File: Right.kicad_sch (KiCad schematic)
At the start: 27 parts, among them J2 Conn_01x02, J4 USB_B_Micro, U1 NCP1117-3.3_SOT223, U2 W25Q128JVS, U3 RP2040, Y1 ECS-120-8-33-JGN-TR3

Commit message: Schematic mostly finished
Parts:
- removed J4: USB_B_Micro, symbol arisu-split:USB_B_Micro
- removed Y1: ECS-120-8-33-JGN-TR3, Crystal:Crystal_SMD_EuroQuartz_MT-4Pin_3.2x2.5mm, symbol Device:Crystal
- added J4: 10103594-0001LF, arisu-split:USB_Micro-B_Amphenol_10103594-0001LF_Horizontal, symbol arisu-split:10103594-0001LF
- added Y1: ECS-120-8-33-JGN-TR3, Crystal:Crystal_SMD_EuroQuartz_MT-4Pin_3.2x2.5mm, symbol Device:Crystal_GND24
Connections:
- net GND_R: now also J4.5 (GND), J4.6 (Shield), Y1.2, Y1.4
- net USB_D+: now also J4.3 (D+)
- net USB_D-: now also J4.2 (D-)
- net XIN: now also Y1.1
- net at C2.1, R3.2: now also Y1.3
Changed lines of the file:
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@@
     (effects (font (size 2.54 2.54)) (justify left bottom))
   )
-  (text "12MHz\n" (at 49.53 161.29 0)
+  (text "12MHz\n" (at 50.8 157.48 0)
     (effects (font (size 1.27 1.27)) (justify left bottom))
   )
@@
     (pin "2")
   )
+  (symbol (lib_id "Device:Crystal_GND24") (at 45.72 158.75 270) (unit 1)
+    (in_bom yes) (on_board yes)
+    (property "Reference" "Y1" (id 0) (at 44.45 148.59 90)
+      (effects (font (size 1.27 1.27)) (justify left))
+    )
+    (property "Value" "ECS-120-8-33-JGN-TR3" (id 1) (at 34.29 151.13 90)
+      (effects (font (size 1.27 1.27)) (justify left))
+    )
+    (property "Footprint" "Crystal:Crystal_SMD_EuroQuartz_MT-4Pin_3.2x2.5mm" (id 2) (at 45.72 158.75 0)
+      (effects (font (size 1.27 1.27)) hide)
+    )
+    (property "Datasheet" "~" (id 3) (at 45.72 158.75 0)
+      (effects (font (size 1.27 1.27)) hide)
+    )
+    (pin "1")
+    (pin "2")
+    (pin "3")
+    (pin "4")
+  )
   (symbol (lib_id "Device:C") (at 251.46 33.02 0) (unit 1)
     (in_bom yes) (on_board yes)
@@
     (pin "1")
   )
-  (symbol (lib_id "Device:Crystal") (at 45.72 158.75 270) (unit 1)
-    (in_bom yes) (on_board yes)
-    (property "Reference" "Y1" (id 0) (at 49.0474 157.5816 90)
-      (effects (font (size 1.27 1.27)) (justify left))
-    )
-    (property "Value" "ECS-120-8-33-JGN-TR3" (id 1) (at 34.29 151.13 90)
-      (effects (font (size 1.27 1.27)) (justify left))
-    )
-    (property "Footprint" "Crystal:Crystal_SMD_EuroQuartz_MT-4Pin_3.2x2.5mm" (id 2) (at 45.72 158.75 0)
-      (effects (font (size 1.27 1.27)) hide)
-    )
-    (property "Datasheet" "~" (id 3) (at 45.72 158.75 0)
-      (effects (font (size 1.27 1.27)) hide)
-    )
-    (pin "1")
-    (pin "2")
-  )
   (symbol (lib_id "arisu-split:GND_R") (at 102.87 38.1 0) (unit 1)
     (in_bom yes) (on_board yes) (fields_autoplaced)
@@
     (pin "1")
   )
-  (symbol (lib_id "Device:C") (at 194.31 48.26 0) (unit 1)
-    (in_bom yes) (on_board yes)
-    (property "Reference" "C10" (id 0) (at 197.231 47.0916 0)
-      (effects (font (size 1.27 1.27)) (justify left))
-    )
-    (property "Value" "1u" (id 1) (at 197.231 49.403 0)
-      (effects (font (size 1.27 1.27)) (justify left))
-    )
-    (property "Footprint" "Capacitor_SMD:C_0402_1005Metric" (id 2) (at 195.2752 52.07 0)
-      (effects (font (size 1.27 1.27)) hide)
-    )
-    (property "Datasheet" "~" (id 3) (at 194.31 48.26 0)
-      (effects (font (size 1.27 1.27)) hide)
-    )
-    (pin "1")
-    (pin "2")
-  )
-  (symbol (lib_id "Device:C") (at 30.48 163.83 270) (unit 1)
-    (in_bom yes) (on_board yes)
-    (property "Reference" "C2" (id 0) (at 31.6484 166.751 0)
-      (effects (font (size 1.27 1.27)) (justify left))
-    )
-    (property "Value" "30p" (id 1) (at 29.337 166.751 0)
-      (effects (font (size 1.27 1.27)) (justify left))
-    )
-    (property "Footprint" "Capacitor_SMD:C_0402_1005Metric" (id 2) (at 26.67 164.7952 0)
-      (effects (font (size 1.27 1.27)) hide)
-    )
-    (property "Datasheet" "~" (id 3) (at 30.48 163.83 0)
-      (effects (font (size 1.27 1.27)) hide)
-    )
-    (pin "1")
-    (pin "2")
-  )
-  (symbol (lib_id "arisu-split:+3V3_R") (at 102.87 26.67 0) (unit 1)
-    (in_bom yes) (on_board yes) (fields_autoplaced)
-    (property "Reference" "#PWR0103" (id 0) (at 102.87 30.48 0)
-      (effects (font (size 1.27 1.27)) hide)
-    )
-    (property "Value" "+3V3_R" (id 1) (at 102.87 23.0942 0))
-    (property "Footprint" "" (id 2) (at 102.87 26.67 0)
-      (effects (font (size 1.27 1.27)) hide)
-    )
-    (property "Datasheet" "" (id 3) (at 102.87 26.67 0)
-      (effects (font (size 1.27 1.27)) hide)
-    )
-    (pin "1")
-  )
-  (symbol (lib_id "arisu-split:GND_R") (at 262.89 40.64 0) (unit 1)
-    (in_bom yes) (on_board yes) (fields_autoplaced)
-    (property "Reference" "#PWR0124" (id 0) (at 262.89 46.99 0)
-      (effects (font (size 1.27 1.27)) hide)
-    )
-    (property "Value" "GND_R" (id 1) (at 262.89 45.0834 0))
-    (property "Footprint" "" (id 2) (at 262.89 40.64 0)
-      (effects (font (size 1.27 1.27)) hide)
-    )
-    (property "Datasheet" "" (id 3) (at 262.89 40.64 0)
-      (effects (font (size 1.27 1.27)) hide)
-    )
-    (pin "1")
-  )
-  (symbol (lib_id "arisu-split:GND_R") (at 24.13 166.37 0) (unit 1)
-    (in_bom yes) (on_board yes) (fields_autoplaced)
-    (property "Reference" "#PWR0127" (id 0) (at 24.13 172.72 0)
-      (effects (font (size 1.27 1.27)) hide)
-    )
-    (property "Value" "GND_R" (id 1) (at 24.13 170.8134 0))
-    (property "Footprint" "" (id 2) (at 24.13 166.37 0)
-      (effects (font (size 1.27 1.27)) hide)
-    )
-    (property "Datasheet" "" (id 3) (at 24.13 166.37 0)
-      (effects (font (size 1.27 1.27)) hide)
-    )
-    (pin "1")
-  )
-  (symbol (lib_id "arisu-split:USB_B_Micro") (at 24.13 30.48 0) (unit 1)
+  (symbol (lib_id "arisu-split:10103594-0001LF") (at 24.13 30.48 0) (unit 1)
     (in_bom yes) (on_board yes) (fields_autoplaced)
     (property "Reference" "J4" (id 0) (at 24.13 19.1602 0))
-    (property "Value" "USB_B_Micro" (id 1) (at 24.13 21.6971 0))
-    (property "Footprint" "" (id 2) (at 27.94 31.75 0)
+    (property "Value" "10103594-0001LF" (id 1) (at 24.13 21.6971 0))
+    (property "Footprint" "arisu-split:USB_Micro-B_Amphenol_10103594-0001LF_Horizontal" (id 2) (at 27.94 31.75 0)
       (effects (font (size 1.27 1.27)) hide)
     )
@@
     (pin "6")
   )
+  (symbol (lib_id "Device:C") (at 194.31 48.26 0) (unit 1)
+    (in_bom yes) (on_board yes)
+    (property "Reference" "C10" (id 0) (at 197.231 47.0916 0)
+      (effects (font (size 1.27 1.27)) (justify left))
+    )
+    (property "Value" "1u" (id 1) (at 197.231 49.403 0)
+      (effects (font (size 1.27 1.27)) (justify left))
+    )
+    (property "Footprint" "Capacitor_SMD:C_0402_1005Metric" (id 2) (at 195.2752 52.07 0)
+      (effects (font (size 1.27 1.27)) hide)
+    )
+    (property "Datasheet" "~" (id 3) (at 194.31 48.26 0)
+      (effects (font (size 1.27 1.27)) hide)
+    )
+    (pin "1")
+    (pin "2")
+  )
+  (symbol (lib_id "Device:C") (at 30.48 163.83 270) (unit 1)
+    (in_bom yes) (on_board yes)
+    (property "Reference" "C2" (id 0) (at 31.6484 166.751 0)
+      (effects (font (size 1.27 1.27)) (justify left))
+    )
+    (property "Value" "30p" (id 1) (at 29.337 166.751 0)
+      (effects (font (size 1.27 1.27)) (justify left))
+    )
+    (property "Footprint" "Capacitor_SMD:C_0402_1005Metric" (id 2) (at 26.67 164.7952 0)
+      (effects (font (size 1.27 1.27)) hide)
+    )
+    (property "Datasheet" "~" (id 3) (at 30.48 163.83 0)
+      (effects (font (size 1.27 1.27)) hide)
+    )
+    (pin "1")
+    (pin "2")
+  )
+  (symbol (lib_id "arisu-split:+3V3_R") (at 102.87 26.67 0) (unit 1)
+    (in_bom yes) (on_board yes) (fields_autoplaced)
+    (property "Reference" "#PWR0103" (id 0) (at 102.87 30.48 0)
+      (effects (font (size 1.27 1.27)) hide)
+    )
+    (property "Value" "+3V3_R" (id 1) (at 102.87 23.0942 0))
+    (property "Footprint" "" (id 2) (at 102.87 26.67 0)
+      (effects (font (size 1.27 1.27)) hide)
+    )
+    (property "Datasheet" "" (id 3) (at 102.87 26.67 0)
+      (effects (font (size 1.27 1.27)) hide)
+    )
+    (pin "1")
+  )
+  (symbol (lib_id "arisu-split:GND_R") (at 262.89 40.64 0) (unit 1)
+    (in_bom yes) (on_board yes) (fields_autoplaced)
+    (property "Reference" "#PWR0124" (id 0) (at 262.89 46.99 0)
+      (effects (font (size 1.27 1.27)) hide)
+    )
+    (property "Value" "GND_R" (id 1) (at 262.89 45.0834 0))
+    (property "Footprint" "" (id 2) (at 262.89 40.64 0)
+      (effects (font (size 1.27 1.27)) hide)
+    )
+    (property "Datasheet" "" (id 3) (at 262.89 40.64 0)
+      (effects (font (size 1.27 1.27)) hide)
+    )
+    (pin "1")
+  )
+  (symbol (lib_id "arisu-split:GND_R") (at 24.13 166.37 0) (unit 1)
+    (in_bom yes) (on_board yes) (fields_autoplaced)
+    (property "Reference" "#PWR0127" (id 0) (at 24.13 172.72 0)
+      (effects (font (size 1.27 1.27)) hide)
+    )
+    (property "Value" "GND_R" (id 1) (at 24.13 170.8134 0))
+    (property "Footprint" "" (id 2) (at 24.13 166.37 0)
+      (effects (font (size 1.27 1.27)) hide)
+    )
+    (property "Datasheet" "" (id 3) (at 24.13 166.37 0)
+      (effects (font (size 1.27 1.27)) hide)
+    )
+    (pin "1")
+  )
   (symbol (lib_id "Device:R") (at 215.9 63.5 270) (unit 1)
     (in_bom yes) (on_board yes)
@@
     (pin "2")
   )
+  (symbol (lib_id "arisu-split:GND_R") (at 40.64 158.75 0) (unit 1)
+    (in_bom yes) (on_board yes)
+    (property "Reference" "#PWR0134" (id 0) (at 40.64 165.1 0)
+      (effects (font (size 1.27 1.27)) hide)
+    )
+    (property "Value" "GND_R" (id 1) (at 40.64 162.56 0))
+    (property "Footprint" "" (id 2) (at 40.64 158.75 0)
+      (effects (font (size 1.27 1.27)) hide)
+    )
+    (property "Datasheet" "" (id 3) (at 40.64 158.75 0)
+      (effects (font (size 1.27 1.27)) hide)
+    )
+    (pin "1")
+  )
   (symbol (lib_id "Device:C") (at 228.6 33.02 0) (unit 1)
     (in_bom yes) (on_board yes)
@@
     (pin "2")
   )
+  (symbol (lib_id "arisu-split:GND_R") (at 50.8 158.75 0) (unit 1)
+    (in_bom yes) (on_board yes)
+    (property "Reference" "#PWR0133" (id 0) (at 50.8 165.1 0)
+      (effects (font (size 1.27 1.27)) hide)
+    )
+    (property "Value" "GND_R" (id 1) (at 50.8 162.56 0))
+    (property "Footprint" "" (id 2) (at 50.8 158.75 0)
+      (effects (font (size 1.27 1.27)) hide)
+    )
+    (property "Datasheet" "" (id 3) (at 50.8 158.75 0)
+      (effects (font (size 1.27 1.27)) hide)
+    )
+    (pin "1")
+  )
   (symbol (lib_id "arisu-split:GND_R") (at 21.59 43.18 0) (unit 1)

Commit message: more layout, and some 3d files
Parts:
- removed U1: NCP1117-3.3_SOT223, Package_TO_SOT_SMD:SOT-223-3_TabPin2, symbol Regulator_Linear:NCP1117-3.3_SOT223
- added C35: 10n, Capacitor_SMD:C_0603_1608Metric, symbol Device:C
- added U9: LM1117-3.3, Package_TO_SOT_SMD:SOT-223-3_TabPin2, symbol Regulator_Linear:LM1117-3.3
- C4, R1, R2, R4, R5: footprint Capacitor_SMD:C_0402_1005Metric -> Capacitor_SMD:C_0603_1608Metric
- U2: footprint Package_SO:SOIC-8_5.23x5.23mm_P1.27mm -> arisu-split:SOIC-8_5.23x5.23mm_P1.27mm
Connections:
- net row2 is gone; now on net col4: U3.13 (GPIO10)
- net +3V3_R: now also C35.1, U9.2 (VO)
- net +5R: now also U9.3 (VI)
- net GND_R: now also C35.2, U9.1 (GND)
- net RX_R: now also U3.32 (GPIO21); no longer U3.28 (GPIO17)
- net TX_R: now also U3.31 (GPIO20); no longer U3.27 (GPIO16)
- net col0: now also U3.6 (GPIO4); no longer U3.2 (GPIO0)
- net col1: now also U3.7 (GPIO5); no longer U3.3 (GPIO1)
- net col2: now also U3.8 (GPIO6); no longer U3.4 (GPIO2)
- net col3: now also U3.12 (GPIO9); no longer U3.5 (GPIO3)
- net col4: no longer U3.6 (GPIO4)
- net col5: now also U3.14 (GPIO11); no longer U3.7 (GPIO5)
- net col6: now also U3.16 (GPIO13); no longer U3.8 (GPIO6)
- net col7: now also U3.15 (GPIO12); no longer U3.9 (GPIO7)
- net row0: now also U3.18 (GPIO15); no longer U3.11 (GPIO8)
- net row1: now also U3.17 (GPIO14); no longer U3.12 (GPIO9)
- net row3: now also U3.3 (GPIO1); no longer U3.14 (GPIO11)
- net row4: now also U3.2 (GPIO0); no longer U3.15 (GPIO12)
- net USB_C_D-: now reaches R5.2, U3.46 (USB_DM)
- net USB_C_D+: now reaches R4.2, U3.47 (USB_DP)
- no-connect marks 17 -> 18

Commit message: Started work on e.eco case cutout
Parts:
- added H5, H6, H8, H?: MountingHole_Pad, MountingHole:MountingHole_3.2mm_M3_Pad_Via, symbol Mechanical:MountingHole_Pad
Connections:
- net GND_R: now also H5.1, H6.1, H8.1, H?.1
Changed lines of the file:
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@@
     (pin "2")
+  )
+  (symbol (lib_id "Mechanical:MountingHole_Pad") (at 132.08 177.8 0) (unit 1)
+    (in_bom yes) (on_board yes) (fields_autoplaced)
+    (property "Reference" "H5" (id 0) (at 134.62 175.6953 0)
+      (effects (font (size 1.27 1.27)) (justify left))
+    )
+    (property "Value" "MountingHole_Pad" (id 1) (at 134.62 178.2322 0)
+      (effects (font (size 1.27 1.27)) (justify left))
+    )
+    (property "Footprint" "MountingHole:MountingHole_3.2mm_M3_Pad_Via" (id 2) (at 132.08 177.8 0)
+      (effects (font (size 1.27 1.27)) hide)
+    )
+    (property "Datasheet" "~" (id 3) (at 132.08 177.8 0)
+      (effects (font (size 1.27 1.27)) hide)
+    )
+    (pin "1")
   )
   (symbol (lib_id "Device:R") (at 215.9 71.12 270) (unit 1)
@@
     (pin "2")
   )
+  (symbol (lib_id "Mechanical:MountingHole_Pad") (at 154.94 190.5 0) (unit 1)
+    (in_bom yes) (on_board yes) (fields_autoplaced)
+    (property "Reference" "H8" (id 0) (at 157.48 188.3953 0)
+      (effects (font (size 1.27 1.27)) (justify left))
+    )
+    (property "Value" "MountingHole_Pad" (id 1) (at 157.48 190.9322 0)
+      (effects (font (size 1.27 1.27)) (justify left))
+    )
+    (property "Footprint" "MountingHole:MountingHole_3.2mm_M3_Pad_Via" (id 2) (at 154.94 190.5 0)
+      (effects (font (size 1.27 1.27)) hide)
+    )
+    (property "Datasheet" "~" (id 3) (at 154.94 190.5 0)
+      (effects (font (size 1.27 1.27)) hide)
+    )
+    (pin "1")
+  )
   (symbol (lib_id "arisu-split:+3V3_R") (at 102.87 26.67 0) (unit 1)
     (in_bom yes) (on_board yes) (fields_autoplaced)
@@
     )
     (property "Datasheet" "" (id 3) (at 24.13 166.37 0)
+      (effects (font (size 1.27 1.27)) hide)
+    )
+    (pin "1")
+  )
+  (symbol (lib_id "arisu-split:GND_R") (at 154.94 180.34 0) (unit 1)
+    (in_bom yes) (on_board yes) (fields_autoplaced)
+    (property "Reference" "#PWR?" (id 0) (at 154.94 186.69 0)
+      (effects (font (size 1.27 1.27)) hide)
+    )
+    (property "Value" "GND_R" (id 1) (at 154.94 184.7834 0))
+    (property "Footprint" "" (id 2) (at 154.94 180.34 0)
+      (effects (font (size 1.27 1.27)) hide)
+    )
+    (property "Datasheet" "" (id 3) (at 154.94 180.34 0)
       (effects (font (size 1.27 1.27)) hide)
     )
@@
     (pin "1")
   )
+  (symbol (lib_id "arisu-split:GND_R") (at 132.08 180.34 0) (unit 1)
+    (in_bom yes) (on_board yes) (fields_autoplaced)
+    (property "Reference" "#PWR0156" (id 0) (at 132.08 186.69 0)
+      (effects (font (size 1.27 1.27)) hide)
+    )
+    (property "Value" "GND_R" (id 1) (at 132.08 184.7834 0))
+    (property "Footprint" "" (id 2) (at 132.08 180.34 0)
+      (effects (font (size 1.27 1.27)) hide)
+    )
+    (property "Datasheet" "" (id 3) (at 132.08 180.34 0)
+      (effects (font (size 1.27 1.27)) hide)
+    )
+    (pin "1")
+  )
   (symbol (lib_id "Device:C") (at 30.48 153.67 270) (unit 1)
     (in_bom yes) (on_board yes)
@@
     (pin "1")
   )
+  (symbol (lib_id "arisu-split:GND_R") (at 154.94 193.04 0) (unit 1)
+    (in_bom yes) (on_board yes) (fields_autoplaced)
+    (property "Reference" "#PWR0154" (id 0) (at 154.94 199.39 0)
+      (effects (font (size 1.27 1.27)) hide)
+    )
+    (property "Value" "GND_R" (id 1) (at 154.94 197.4834 0))
+    (property "Footprint" "" (id 2) (at 154.94 193.04 0)
+      (effects (font (size 1.27 1.27)) hide)
+    )
+    (property "Datasheet" "" (id 3) (at 154.94 193.04 0)
+      (effects (font (size 1.27 1.27)) hide)
+    )
+    (pin "1")
+  )
   (symbol (lib_id "Device:C") (at 228.6 33.02 0) (unit 1)
     (in_bom yes) (on_board yes)
@@
     )
     (property "Datasheet" "" (id 3) (at 50.8 158.75 0)
+      (effects (font (size 1.27 1.27)) hide)
+    )
+    (pin "1")
+  )
+  (symbol (lib_id "Mechanical:MountingHole_Pad") (at 154.94 177.8 0) (unit 1)
+    (in_bom yes) (on_board yes) (fields_autoplaced)
+    (property "Reference" "H?" (id 0) (at 157.48 175.6953 0)
+      (effects (font (size 1.27 1.27)) (justify left))
+    )
+    (property "Value" "MountingHole_Pad" (id 1) (at 157.48 178.2322 0)
+      (effects (font (size 1.27 1.27)) (justify left))
+    )
+    (property "Footprint" "MountingHole:MountingHole_3.2mm_M3_Pad_Via" (id 2) (at 154.94 177.8 0)
+      (effects (font (size 1.27 1.27)) hide)
+    )
+    (property "Datasheet" "~" (id 3) (at 154.94 177.8 0)
       (effects (font (size 1.27 1.27)) hide)
     )
@@
     (pin "9")
   )
+  (symbol (lib_id "arisu-split:GND_R") (at 132.08 193.04 0) (unit 1)
+    (in_bom yes) (on_board yes) (fields_autoplaced)
+    (property "Reference" "#PWR0155" (id 0) (at 132.08 199.39 0)
+      (effects (font (size 1.27 1.27)) hide)
+    )
+    (property "Value" "GND_R" (id 1) (at 132.08 197.4834 0))
+    (property "Footprint" "" (id 2) (at 132.08 193.04 0)
+      (effects (font (size 1.27 1.27)) hide)
+    )
+    (property "Datasheet" "" (id 3) (at 132.08 193.04 0)
+      (effects (font (size 1.27 1.27)) hide)
+    )
+    (pin "1")
+  )
+  (symbol (lib_id "Mechanical:MountingHole_Pad") (at 132.08 190.5 0) (unit 1)
+    (in_bom yes) (on_board yes) (fields_autoplaced)
+    (property "Reference" "H6" (id 0) (at 134.62 188.3953 0)
+      (effects (font (size 1.27 1.27)) (justify left))
+    )
+    (property "Value" "MountingHole_Pad" (id 1) (at 134.62 190.9322 0)
+      (effects (font (size 1.27 1.27)) (justify left))
+    )
+    (property "Footprint" "MountingHole:MountingHole_3.2mm_M3_Pad_Via" (id 2) (at 132.08 190.5 0)
+      (effects (font (size 1.27 1.27)) hide)
+    )
+    (property "Datasheet" "~" (id 3) (at 132.08 190.5 0)
+      (effects (font (size 1.27 1.27)) hide)
+    )
+    (pin "1")
+  )
   (sheet (at 223.52 92.71) (size 12.7 5.08)

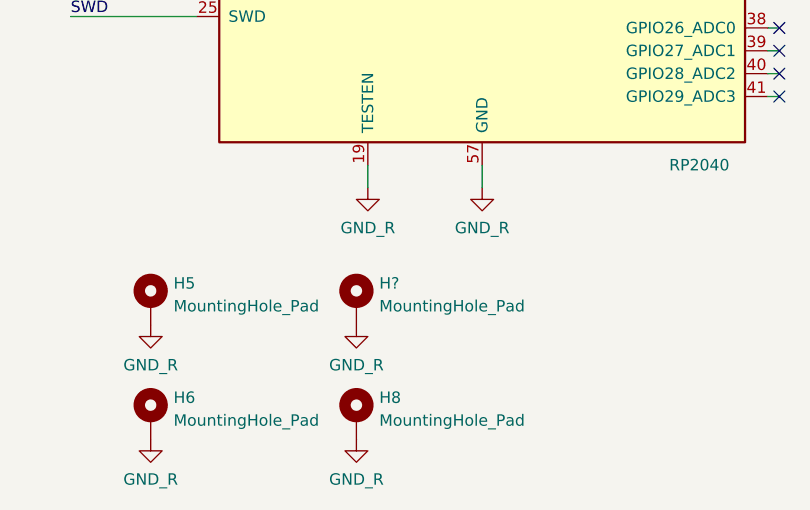
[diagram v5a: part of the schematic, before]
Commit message: Add cutout drawings
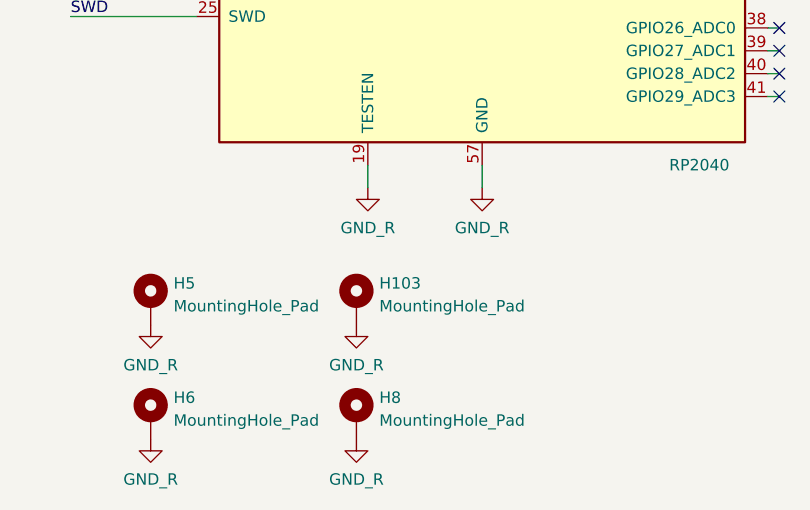
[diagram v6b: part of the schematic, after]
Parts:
- gave numbers to parts that had none: 1
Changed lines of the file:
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@@
   (symbol (lib_id "arisu-split:GND_R") (at 154.94 180.34 0) (unit 1)
     (in_bom yes) (on_board yes) (fields_autoplaced)
-    (property "Reference" "#PWR?" (id 0) (at 154.94 186.69 0)
+    (property "Reference" "#PWR0152" (id 0) (at 154.94 186.69 0)
       (effects (font (size 1.27 1.27)) hide)
     )
@@
   (symbol (lib_id "Mechanical:MountingHole_Pad") (at 154.94 177.8 0) (unit 1)
     (in_bom yes) (on_board yes) (fields_autoplaced)
-    (property "Reference" "H?" (id 0) (at 157.48 175.6953 0)
-      (effects (font (size 1.27 1.27)) (justify left))
-    )
+    (property "Reference" "H103" (id 0) (at 157.48 175.6953 0)
+      (effects (font (size 1.27 1.27)) (justify left))
+    )

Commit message: left side of keyboard finished for the time being
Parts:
- J2: footprint Connector_PinHeader_2.54mm:PinHeader_1x02_P2.54mm_Vertical -> Connector_PinHeader_2.54mm:PinHeader_1x02_P2.54mm_Horizontal
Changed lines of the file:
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@@
     (property "Reference" "J2" (id 0) (at 20.32 97.79 0))
     (property "Value" "Conn_01x02" (id 1) (at 20.32 107.95 0))
-    (property "Footprint" "Connector_PinHeader_2.54mm:PinHeader_1x02_P2.54mm_Vertical" (id 2) (at 21.59 101.6 0)
+    (property "Footprint" "Connector_PinHeader_2.54mm:PinHeader_1x02_P2.54mm_Horizontal" (id 2) (at 21.59 101.6 0)
       (effects (font (size 1.27 1.27)) hide)
     )
